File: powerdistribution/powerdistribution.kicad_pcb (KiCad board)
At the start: 4 copper layers, 110 x 75 mm, 116 parts, among them IC1 NCP718ASNADJT1G, J1 282837-2, J2 282837-2, J3 ESQ-113-12-G-D, J4 XT60-M, J6 Conn_01x02, M1 Motor_Servo, M2 Motor_Servo, Q3 SI7232DN-T1-GE3, U10 TPS1HC30BQPWPRQ1, U11 S2P-VH, U3 AP64501QSP-13, U4 AP64501QSP-13, U5 TPS1HC30BQPWPRQ1, U6 TPS1HC30BQPWPRQ1, U9 AP64501QSP-13

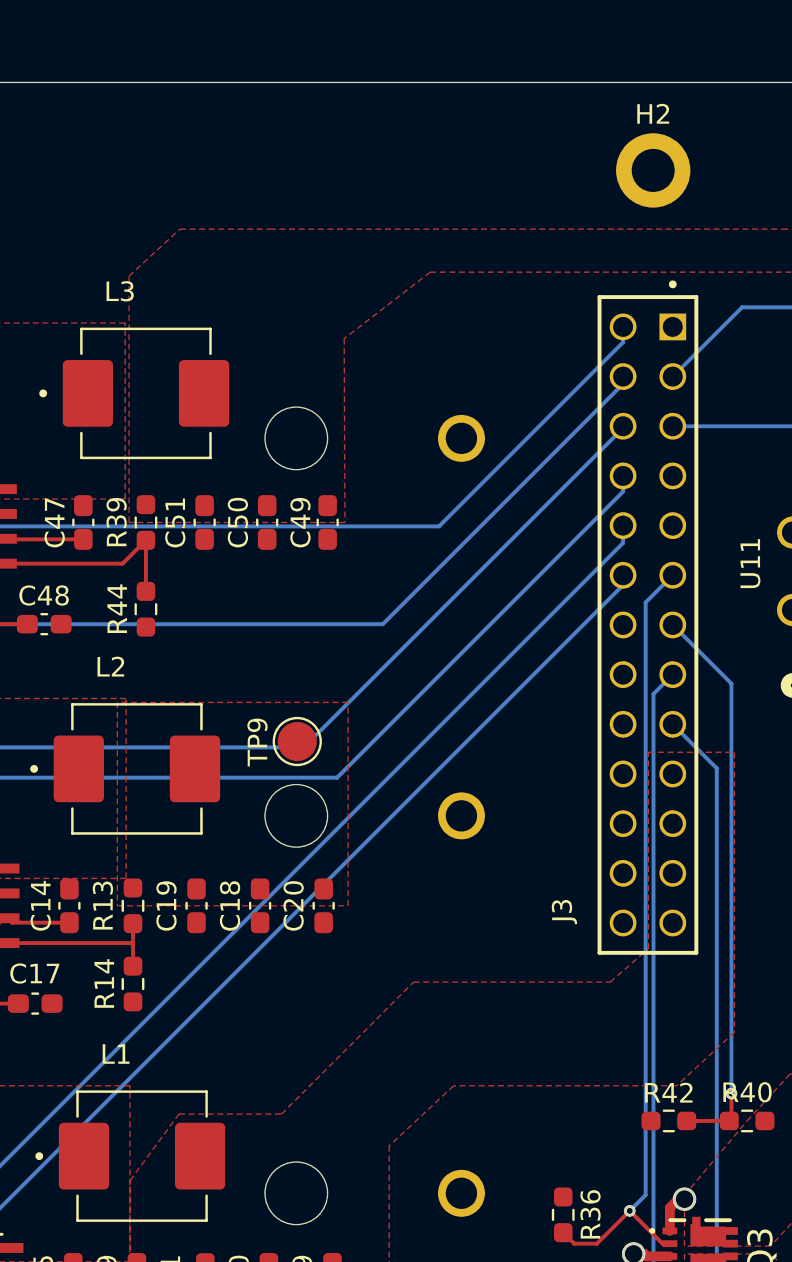
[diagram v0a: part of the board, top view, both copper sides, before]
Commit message: changed coax diodes to 0603, reconfigure conn to add 3.3v, added indicator LEDs.
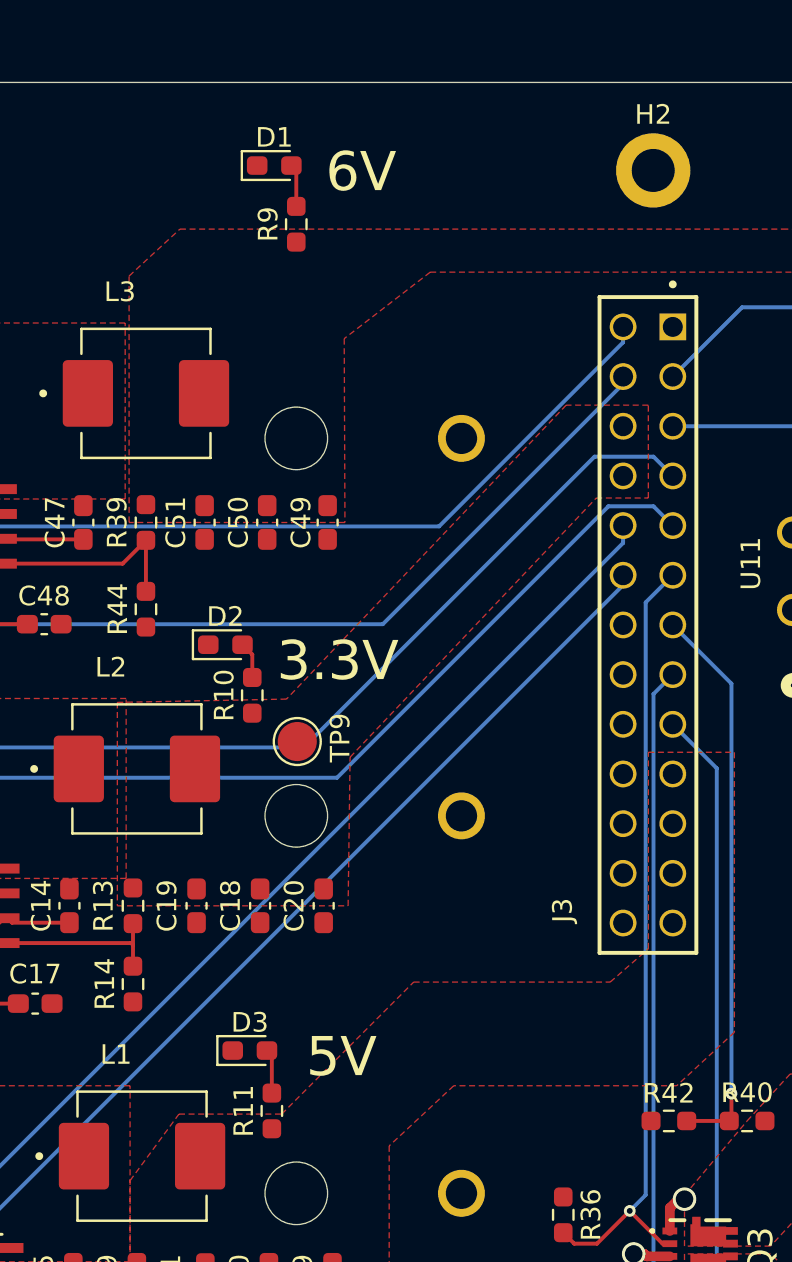
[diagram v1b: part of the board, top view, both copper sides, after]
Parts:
- added D1: LED, LED_SMD:LED_0603_1608Metric_Pad1.05x0.95mm_HandSolder, F.Cu at (105.6, 66.8)
- added D2: LED, LED_SMD:LED_0603_1608Metric_Pad1.05x0.95mm_HandSolder, F.Cu at (103.1, 91.2)
- added D3: LED, LED_SMD:LED_0603_1608Metric_Pad1.05x0.95mm_HandSolder, F.Cu at (104.4, 112.0)
- added R10: R, Resistor_SMD:R_0603_1608Metric_Pad0.98x0.95mm_HandSolder, F.Cu at (104.5, 93.8)
- added R11: R, Resistor_SMD:R_0603_1608Metric_Pad0.98x0.95mm_HandSolder, F.Cu at (105.5, 115.1)
- added R9: R, Resistor_SMD:R_0603_1608Metric_Pad0.98x0.95mm_HandSolder, F.Cu at (106.8, 69.8)
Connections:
- J3 pad 06: /3.3v_fault -> /3.3V
- J3 pad 07: unconnected-(J3-Pad07) -> /3.3v_fault
- J3 pad 08: /3.3v_cursns -> /3.3V
- J3 pad 09: unconnected-(J3-Pad09) -> /3.3v_cursns
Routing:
- net Net-(D3-A): track 0.00 -> 2.28 mm
- net /3.3v_fault: track 73.3 -> 75.6 mm
- net Net-(D1-A): track 0.00 -> 2.19 mm
- net Net-(D2-A): track 0.00 -> 1.88 mm
- net /3.3v_cursns: track 77.8 -> 79.7 mm
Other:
- board text added: "3.3V"
- board text added: "5V"
- board text added: "6V"

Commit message: power board silks
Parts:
- added G***: LOGO, HPRlibrary:HPRLOGOSILK, B.Cu at (131.2, 100.6)
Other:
- board text added: "0 Year Warranty"
- board text added: "dailingw@seas.upenn.edu vidhu@seas.upenn.edu"
